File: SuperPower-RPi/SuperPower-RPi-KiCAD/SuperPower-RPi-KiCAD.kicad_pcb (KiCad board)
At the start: 2 copper layers, 65 x 56.5 mm, 119 parts, among them J1 Raspberry_Pi_2_3, J10 Conn_01x04, J11 QWIIC_Connector, J12 DNP, J13 Conn_01x06, J2 JST-PH, J3 DNP, J4 DNP, J5 DNP, J6 USB_C_Receptacle_USB2.0, J7 Conn_01x03, J8 Conn_02x05_Odd_Even, J9 Conn_01x02, Q1 Q_PMOS_DMP3056L-7_SOT-23, Q2 Q_PMOS_DMP3056L-7_SOT-23, Q3 Q_PMOS_DMP3056L-7_SOT-23, Q6 2N7002-7-F, Q7 Q_PMOS_DMP3056L-7_SOT-23, SW1 Tact, U1 TPS61088, U2 BQ25895RTW, U3 STM32F412RETx, U4 ATtiny85-20SU, U5 ME6210A33M3G, U6 NCP380HMU21AATBG

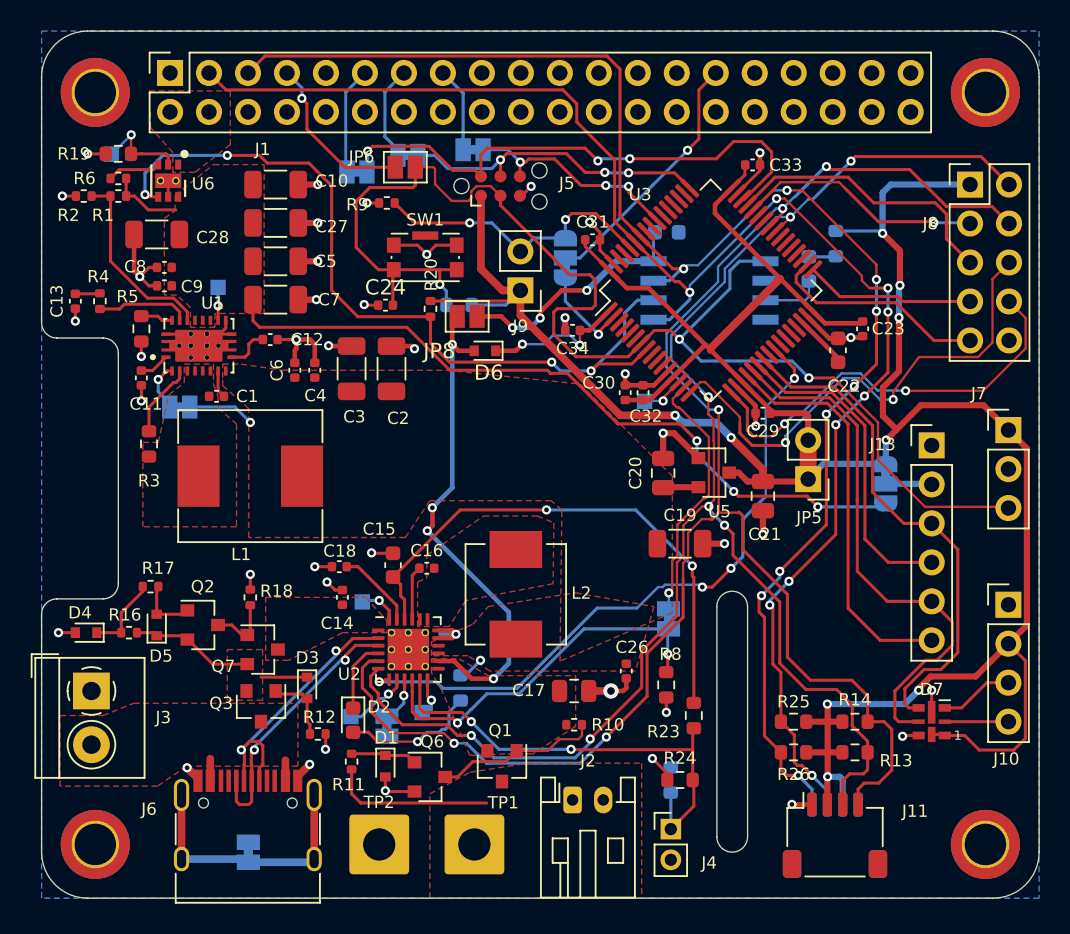
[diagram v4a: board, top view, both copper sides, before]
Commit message: Updated silkscreen
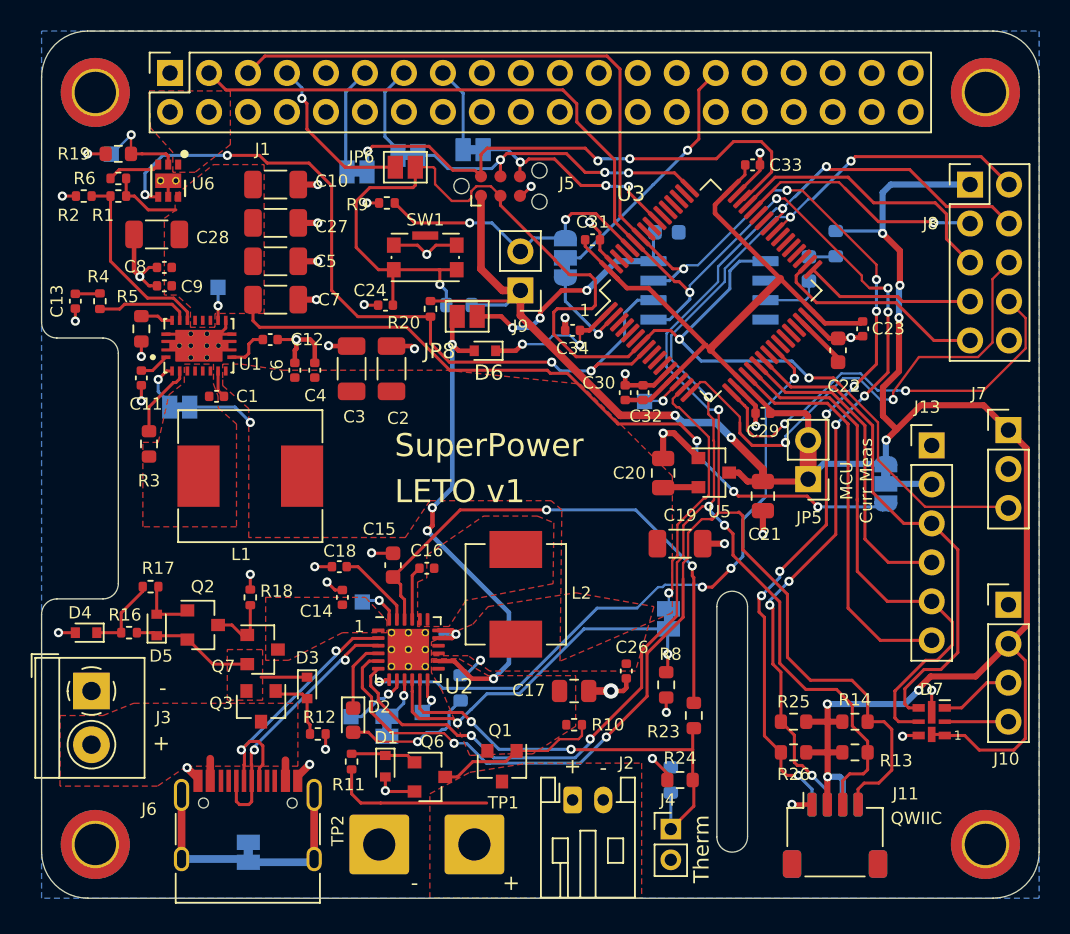
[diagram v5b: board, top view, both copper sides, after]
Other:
- board text added: "+"
- board text added: "-"
- board text added: "1"
- board text added: "3.3V"
- board text added: "5V"
- board text added: "LETO v1"
- board text added: "MCU Curr Meas"
- board text added: "QWIIC"
- board text added: "SuperPower"
- board text added: "Therm"
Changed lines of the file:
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@@
   (general
     (thickness 1.6)
-    (drawings 40)
+    (drawings 55)
     (tracks 1190)
     (zones 0)
@@
   (page A4)
   (layers
-    (0 F.Cu signal)
+    (0 F.Cu signal hide)
     (31 B.Cu signal)
     (34 B.Paste user)
     (35 F.Paste user hide)
     (36 B.SilkS user)
-    (37 F.SilkS user)
+    (37 F.SilkS user hide)
     (38 B.Mask user hide)
     (39 F.Mask user hide)
@@
     (45 Margin user hide)
     (46 B.CrtYd user hide)
-    (47 F.CrtYd user)
+    (47 F.CrtYd user hide)
     (48 B.Fab user hide)
     (49 F.Fab user hide)
   )
   (setup
-    (last_trace_width 0.5)
+    (last_trace_width 0.2)
     (user_trace_width 0.2)
     (user_trace_width 0.3)
@@
     (tags capacitor)
     (attr smd)
-    (fp_text reference C24 (at 0 -1.16) (layer F.SilkS)
-      (effects (font (size 1 1) (thickness 0.15)))
+    (fp_text reference C24 (at -1.01 -0.96) (layer F.SilkS)
+      (effects (font (size 0.8 0.8) (thickness 0.15)))
     )
     (fp_text value 0.1uF (at 0 1.16) (layer F.Fab)
@@
     (tags "solder jumper open")
     (attr virtual)
-    (fp_text reference JP11 (at 0 1.8) (layer B.SilkS)
+    (fp_text reference JP11 (at -1.68 -1.97) (layer B.SilkS)
       (effects (font (size 1 1) (thickness 0.15)) (justify mirror))
     )
@@
     (tags "solder jumper open")
     (attr virtual)
-    (fp_text reference JP10 (at 0 1.8) (layer B.SilkS)
+    (fp_text reference JP10 (at -0.33 -2) (layer B.SilkS)
       (effects (font (size 1 1) (thickness 0.15)) (justify mirror))
     )
@@
     (tags "solder jumper open")
     (attr virtual)
-    (fp_text reference JP9 (at 0 1.8) (layer B.SilkS)
+    (fp_text reference JP9 (at 1.45 -1.92) (layer B.SilkS)
       (effects (font (size 1 1) (thickness 0.15)) (justify mirror))
     )
@@
     (tags resistor)
     (attr smd)
-    (fp_text reference R20 (at 2.22 0.04 270) (layer F.SilkS)
+    (fp_text reference R20 (at -0.9 -1.74) (layer F.SilkS)
       (effects (font (size 0.8 0.8) (thickness 0.15)))
     )
@@
     (attr smd)
     (fp_text reference C25 (at 0 -1.43) (layer B.SilkS)
-      (effects (font (size 1 1) (thickness 0.15)) (justify mirror))
+      (effects (font (size 0.8 0.8) (thickness 0.15)) (justify mirror))
     )
     (fp_text value DNP (at 0 -1.43) (layer B.Fab)
@@
     (descr "JST PH series connector, S2B-PH-K (http://www.jst-mfg.com/product/pdf/eng/ePH.pdf), generated with kicad-footprint-generator")
     (tags "connector JST PH top entry")
-    (fp_text reference J2 (at 1 -2.55) (layer F.SilkS)
+    (fp_text reference J2 (at 3.5 -2.4) (layer F.SilkS)
       (effects (font (size 0.8 0.8) (thickness 0.15)))
     )
@@
     (tags "QFN NoLead")
     (attr smd)
-    (fp_text reference U2 (at -3.85 1.6) (layer F.SilkS)
-      (effects (font (size 0.8 0.8) (thickness 0.15)))
+    (fp_text reference U2 (at 3.3 2.4) (layer F.SilkS)
+      (effects (font (size 1 1) (thickness 0.15)))
     )
     (fp_text value BQ25895RTW (at 0 3.32) (layer F.Fab)
@@
     (fp_arc (start 1.35 -0.3) (end 1.35 -1) (angle 90) (layer B.SilkS) (width 0.12))
     (fp_arc (start 1.35 0.3) (end 2.05 0.3) (angle 90) (layer B.SilkS) (width 0.12))
-    (fp_text user 1 (at -2.6 0 90) (layer B.SilkS)
-      (effects (font (size 0.8 0.8) (thickness 0.15)) (justify mirror))
-    )
-    (fp_text user 3 (at 2.6 0 90) (layer B.SilkS)
-      (effects (font (size 0.8 0.8) (thickness 0.15)) (justify mirror))
-    )
     (pad 1 smd custom (at -1.3 0 270) (size 1 0.5) (layers B.Cu B.Mask)
       (net 11 +3V3) (zone_connect 2)
@@
     (descr "Through hole straight pin header, 1x06, 2.54mm pitch, single row")
     (tags "Through hole pin header THT 1x06 2.54mm single row")
-    (fp_text reference J13 (at -3.2 -0.06) (layer F.SilkS)
+    (fp_text reference J13 (at -0.3 -2.5) (layer F.SilkS)
       (effects (font (size 0.8 0.8) (thickness 0.15)))
     )
@@
     (tags capacitor)
     (attr smd)
-    (fp_text reference C20 (at 0 1.8 90) (layer F.SilkS)
+    (fp_text reference C20 (at 0 2.2 180) (layer F.SilkS)
       (effects (font (size 0.8 0.8) (thickness 0.15)))
     )
@@
     (tags capacitor)
     (attr smd)
-    (fp_text reference C14 (at -1.69 -0.34 180) (layer F.SilkS)
+    (fp_text reference C14 (at -0.9 -1.7 180) (layer F.SilkS)
       (effects (font (size 0.8 0.8) (thickness 0.15)))
     )
@@
     (tags "VQFN, exposed pad.")
     (attr smd)
-    (fp_text reference U1 (at 2.78 0.89 180) (layer F.SilkS)
+    (fp_text reference U1 (at -1.2 3.35 180) (layer F.SilkS)
       (effects (font (size 0.8 0.8) (thickness 0.15)))
     )
@@
     (tags "connector JST SH top entry")
     (attr smd)
-    (fp_text reference J12 (at 0 3.98) (layer B.SilkS)
+    (fp_text reference J12 (at -5.1 2.8) (layer B.SilkS)
       (effects (font (size 0.8 0.8) (thickness 0.15)) (justify mirror))
     )
@@
     (tags "connector JST SH top entry")
     (attr smd)
-    (fp_text reference J11 (at 5.22 -1.57) (layer F.SilkS)
+    (fp_text reference J11 (at 4.6 -2.7) (layer F.SilkS)
       (effects (font (size 0.8 0.8) (thickness 0.15)))
     )
@@
     (pad 1 smd rect (at -3.65 1.905 180) (size 1.7 0.65) (layers B.Cu B.Paste B.Mask)
       (net 12 /Pi-MCU/nRESET))
-    (model ${KISYS3DMOD}/Package_SO.3dshapes/SOIJ-8_5.3x5.3mm_P1.27mm.wrl
-      (at (xyz 0 0 0))
-      (scale (xyz 1 1 1))
-      (rotate (xyz 0 0 0))
-    )
   )
   (module Package_QFP:LQFP-64_10x10mm_P0.5mm (layer F.Cu)
@@
     (tags "LQFP QFP")
     (attr smd)
-    (fp_text reference U3 (at 1.166726 -7.672109 180) (layer F.SilkS)
-      (effects (font (size 0.8 0.8) (thickness 0.15)))
+    (fp_text reference U3 (at 0.777817 -8.131728 180) (layer F.SilkS)
+      (effects (font (size 1 1) (thickness 0.15)))
     )
     (fp_text value STM32F412RETx (at 0 7.4 45) (layer F.Fab)
@@
     (tags "connector wire 1.5sqmm")
     (attr virtual)
-    (fp_text reference TP2 (at -0.01 -2.75) (layer F.SilkS)
+    (fp_text reference TP2 (at -2.7 -0.9 90) (layer F.SilkS)
       (effects (font (size 0.8 0.8) (thickness 0.15)))
     )
@@
     (descr "Through hole straight pin header, 1x02, 2.00mm pitch, single row")
     (tags "Through hole pin header THT 1x02 2.00mm single row")
-    (fp_text reference J4 (at 2.5 2.2) (layer F.SilkS)
+    (fp_text reference J4 (at -0.2 -1.9) (layer F.SilkS)
       (effects (font (size 0.8 0.8) (thickness 0.15)))
     )
@@
     )
   )
+  (gr_text 5V (at 105 82.5) (layer B.SilkS)
+    (effects (font (size 0.8 0.8) (thickness 0.15)) (justify mirror))
+  )
+  (gr_text 3.3V (at 104.7 76.8) (layer B.SilkS)
+    (effects (font (size 0.8 0.8) (thickness 0.15)) (justify mirror))
+  )
+  (gr_text "MCU\nCurr Meas" (at 103.1 79.3 90) (layer F.SilkS)
+    (effects (font (size 0.8 0.8) (thickness 0.15)))
+  )
+  (gr_text 1 (at 70.7 88.8) (layer F.SilkS)
+    (effects (font (size 0.8 0.8) (thickness 0.15)))
+  )
+  (gr_text 1 (at 85.4 68.2) (layer F.SilkS)
+    (effects (font (size 0.8 0.8) (thickness 0.15)))
+  )
+  (gr_text Therm (at 93 103.3 90) (layer F.SilkS)
+    (effects (font (size 1 1) (thickness 0.15)))
+  )
+  (gr_text - (at 86.6 98) (layer F.SilkS)
+    (effects (font (size 1 1) (thickness 0.15)))
+  )
+  (gr_text - (at 74.3 105.5) (layer F.SilkS)
+    (effects (font (size 1 1) (thickness 0.15)))
+  )
+  (gr_text + (at 84.6 97.9) (layer F.SilkS)
+    (effects (font (size 1 1) (thickness 0.15)))
+  )
+  (gr_text + (at 80.6 105.5) (layer F.SilkS)
+    (effects (font (size 1 1) (thickness 0.15)))
+  )
+  (gr_text - (at 57.9 92.8) (layer F.SilkS)
+    (effects (font (size 1 1) (thickness 0.15)))
+  )
+  (gr_text + (at 57.8 96.4) (layer F.SilkS)
+    (effects (font (size 1 1) (thickness 0.15)))
+  )
+  (gr_text QWIIC (at 107 101.3) (layer F.SilkS)
+    (effects (font (size 0.8 0.8) (thickness 0.15)))
+  )
+  (gr_text "LETO v1" (at 73 80) (layer F.SilkS)
+    (effects (font (size 1.5 1.5) (thickness 0.2)) (justify left))
+  )
+  (gr_text SuperPower (at 73 77) (layer F.SilkS)
+    (effects (font (size 1.5 1.5) (thickness 0.2)) (justify left))
+  )
   (gr_line (start 58.3 103.9) (end 69.2 103.9) (layer Dwgs.User) (width 0.01))
   (dimension 3.5 (width 0.15) (layer Dwgs.User)
@@
   (segment (start 72.300001 93.499999) (end 72.6 93.2) (width 0.2) (layer B.Cu) (net 105))
   (segment (start 72 93.5) (end 72.300001 93.499999) (width 0.2) (layer B.Cu) (net 105))
-  (segment (start 75.4 94.2) (end 74.8 94.8) (width 0.2) (layer B.Cu) (net 106))
   (segment (start 75.15 92.2625) (end 75.15 93.35) (width 0.2) (layer F.Cu) (net 106))
-  (segment (start 75.4 93.6) (end 75.4 94.2) (width 0.2) (layer B.Cu) (net 106))
   (segment (start 75.15 93.35) (end 75.4 93.6) (width 0.2) (layer F.Cu) (net 106))
   (via (at 75.4 93.6) (size 0.6) (drill 0.3) (layers F.Cu B.Cu) (net 106))
+  (segment (start 75.4 93.8) (end 75.4 93.6) (width 0.2) (layer B.Cu) (net 106))
+  (segment (start 74.8 94.4) (end 75.4 93.8) (width 0.2) (layer B.Cu) (net 106))
   (segment (start 105.17 84.62) (end 108 84.62) (width 0.2) (layer F.Cu) (net 107))
   (segment (start 103.65 83.1) (end 105.17 84.62) (width 0.2) (layer F.Cu) (net 107))
